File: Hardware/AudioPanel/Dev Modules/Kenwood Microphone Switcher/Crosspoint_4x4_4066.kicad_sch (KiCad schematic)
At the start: 14 parts, among them U106 4066, U107 4066, U108 4066, U51 4066, U53 4066, U55 4066

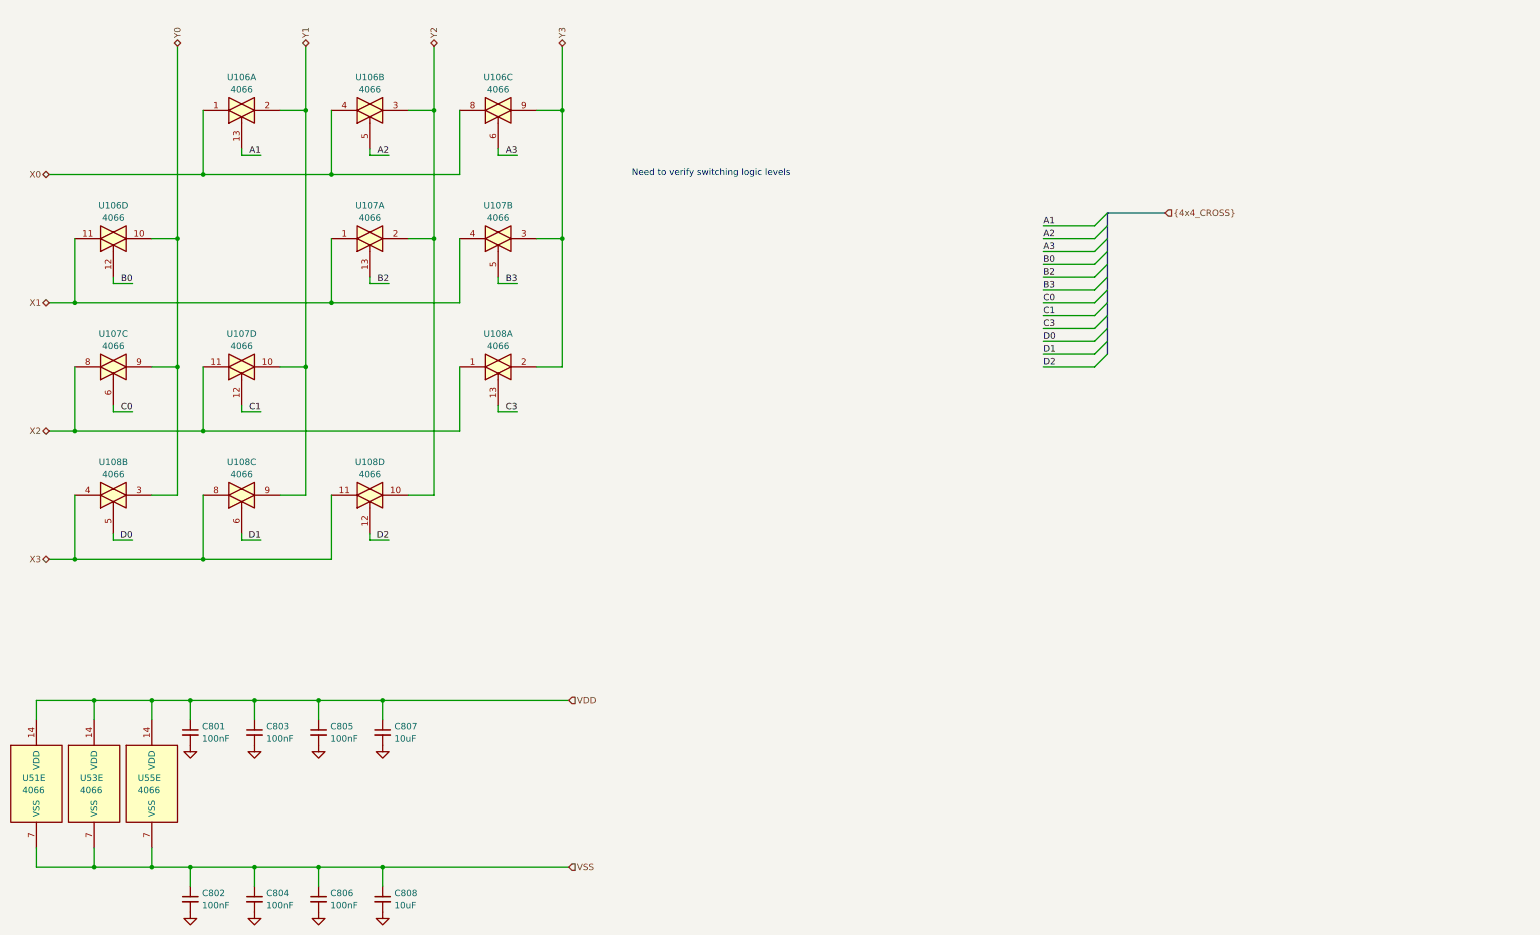
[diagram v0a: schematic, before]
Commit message: Finished most if not all of the microphone dev board
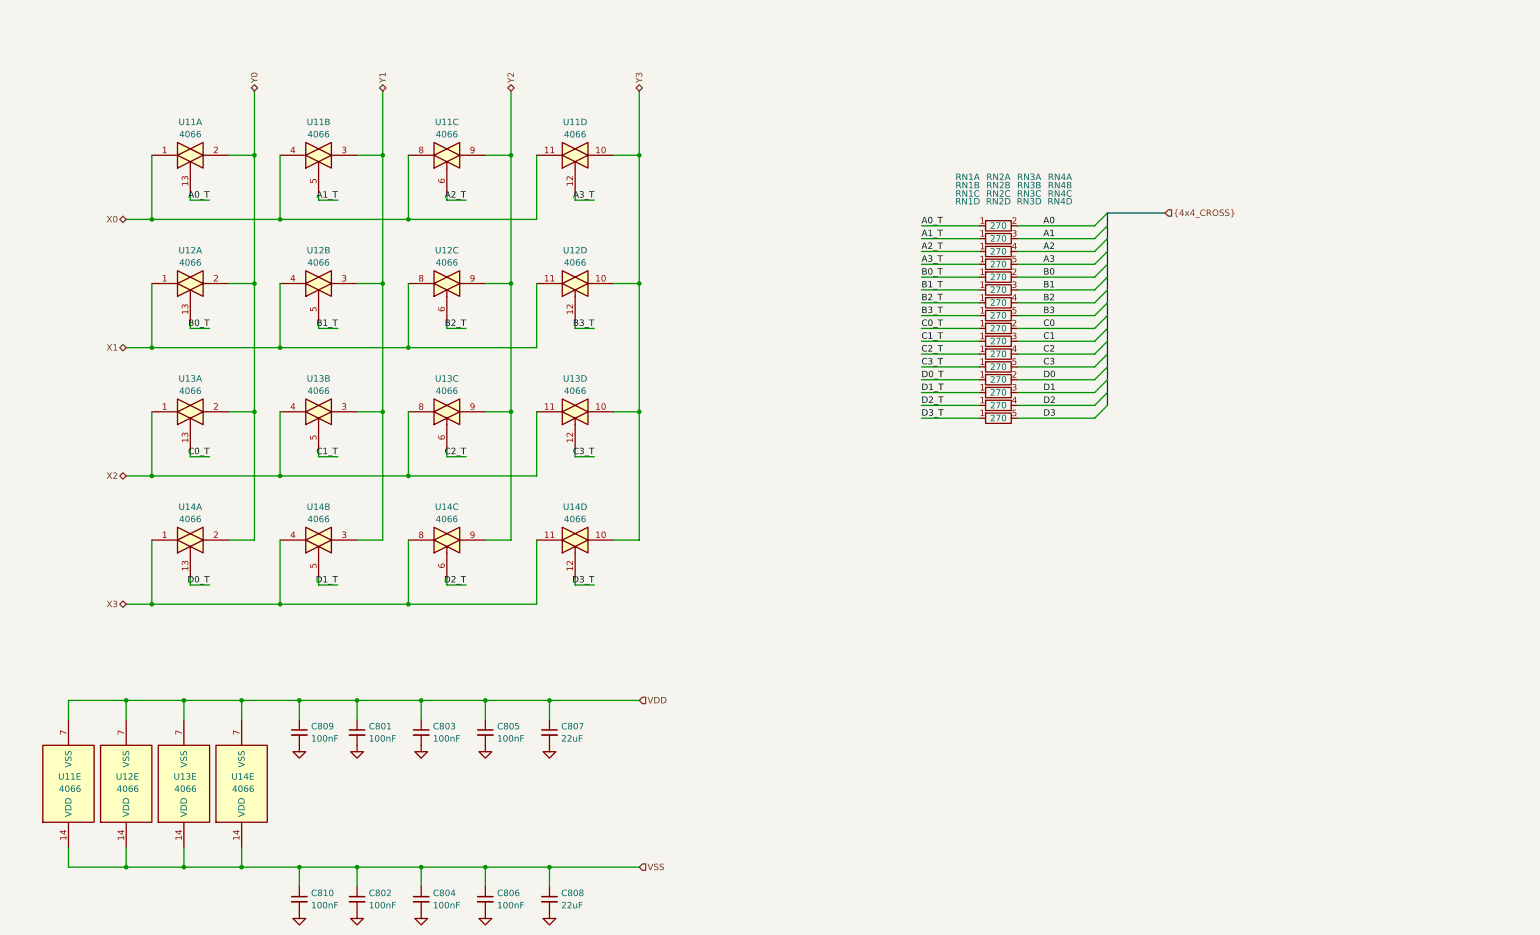
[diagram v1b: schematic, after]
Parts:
- removed U106, U107, U108, U51, U53, U55: 4066, symbol 4xxx:4066
- added C809, C810: 100nF, symbol Device:C_Small
- added RN1, RN2, RN3, RN4: 270, Resistor_THT:R_Array_SIP5, symbol Device:R_Network04_Split
- added U11, U12, U13, U14: 4066, symbol 4xxx:4066
- C807, C808: value 10uF -> 22uF
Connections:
- net A1: now also RN1.3 (R2.2)
- net A2: now also RN1.4 (R3.2)
- net A3: now also RN1.5 (R4.2)
- net B0: now also RN2.2 (R1.2)
- net B2: now also RN2.4 (R3.2)
- net B3: now also RN2.5 (R4.2)
- net C0: now also RN3.2 (R1.2)
- net C1: now also RN3.3 (R2.2)
- net C3: now also RN3.5 (R4.2)
- net D0: now also RN4.2 (R1.2)
- net D1: now also RN4.3 (R2.2)
- net D2: now also RN4.4 (R3.2)
- net GND: now also C809.2, C810.2
- net VDD: now also C809.1, U11.7 (VSS), U12.7 (VSS), U13.7 (VSS), U14.7 (VSS)
- net VSS: now also C810.1, U11.14 (VDD), U12.14 (VDD), U13.14 (VDD), U14.14 (VDD)
- net X0: now also U11.1, U11.11, U11.4, U11.8
- net X1: now also U12.1, U12.11, U12.4, U12.8
- net X2: now also U13.1, U13.11, U13.4, U13.8
- net X3: now also U14.1, U14.11, U14.4, U14.8
- net Y0: now also U11.2, U12.2, U13.2, U14.2
- net Y1: now also U11.3, U12.3, U13.3, U14.3
- net Y2: now also U11.9, U12.9, U13.9, U14.9
- net Y3: now also U11.10, U12.10, U13.10, U14.10
- new net A0: RN1.2 (R1.2)
- new net A0_T: RN1.1 (R1), U11.13
- new net A1_T: RN1.1 (R1), U11.5
- new net A2_T: RN1.1 (R1), U11.6
- new net A3_T: RN1.1 (R1), U11.12
- new net B0_T: RN2.1 (R1), U12.13
- new net B1: RN2.3 (R2.2)
- new net B1_T: RN2.1 (R1), U12.5
- new net B2_T: RN2.1 (R1), U12.6
- new net B3_T: RN2.1 (R1), U12.12
- new net C0_T: RN3.1 (R1), U13.13
- new net C1_T: RN3.1 (R1), U13.5
- new net C2: RN3.4 (R3.2)
- new net C2_T: RN3.1 (R1), U13.6
- new net C3_T: RN3.1 (R1), U13.12
- new net D0_T: RN4.1 (R1), U14.13
- new net D1_T: RN4.1 (R1), U14.5
- new net D2_T: RN4.1 (R1), U14.6
- new net D3: RN4.5 (R4.2)
- new net D3_T: RN4.1 (R1), U14.12
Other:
- note removed: "Need to verify switching logic levels"
- moved on the sheet: C801, C802, C803, C804, C805, C806, C807, C808

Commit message: Removed DAC and buffers for PTT, added PTT LEDs and inverters
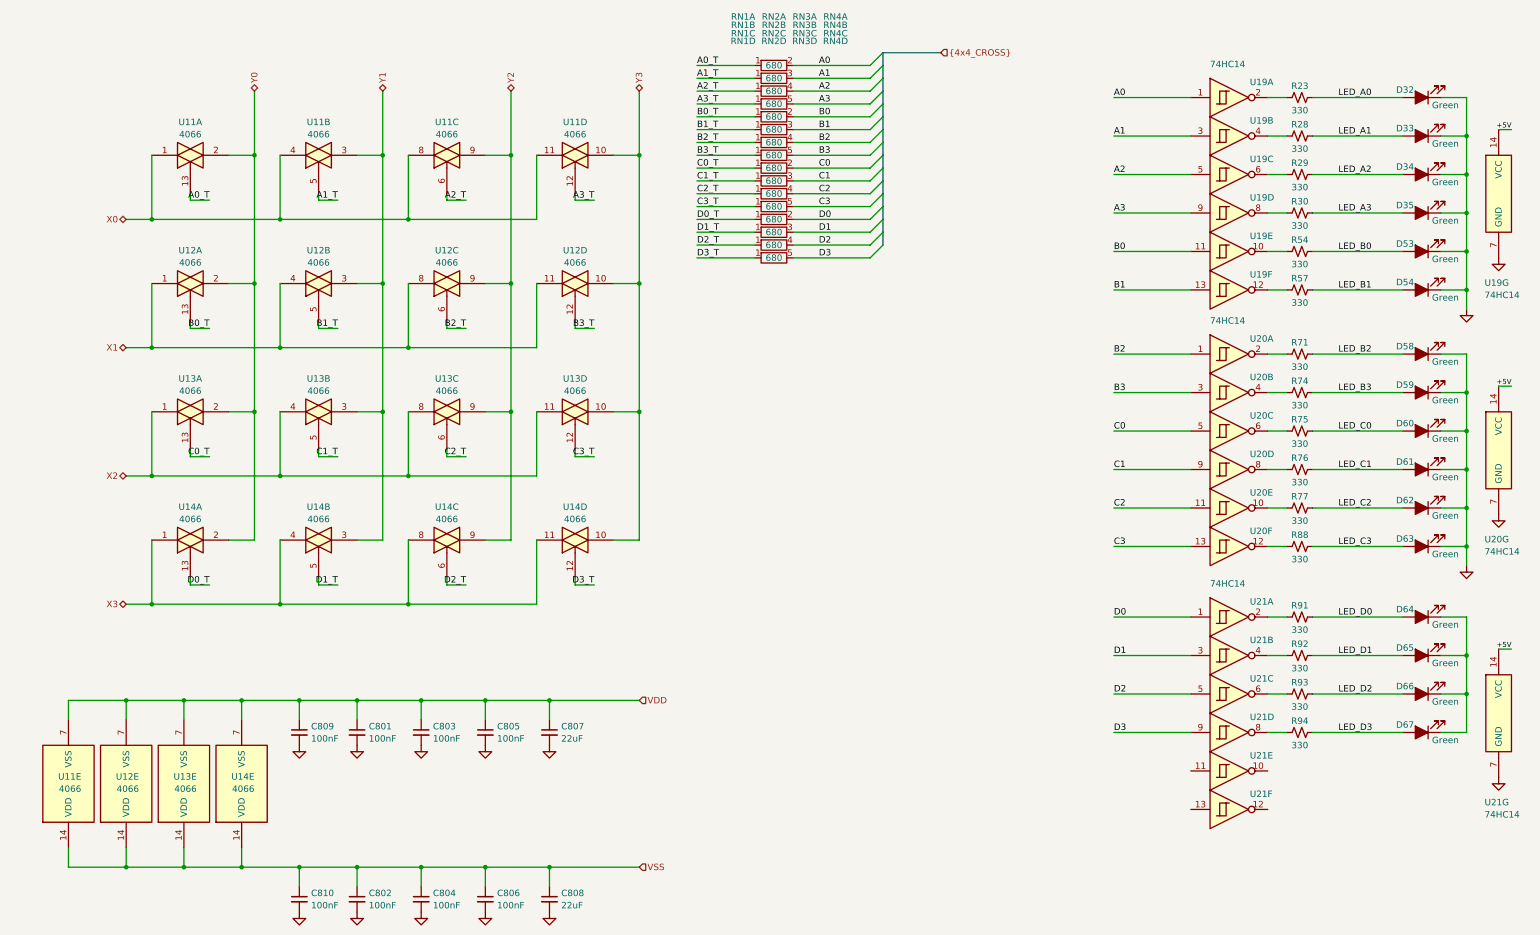
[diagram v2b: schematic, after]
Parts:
- added D32, D33, D34, D35, D53, D54, D58, D59, D60, D61, D62, D63, D64, D65, D66, D67: Green, LED_THT:LED_D5.0mm, symbol Device:LED_Filled
- added R23, R28, R29, R30, R54, R57, R71, R74, R75, R76, R77, R88, R91, R92, R93, R94: 330, symbol Device:R_Small_US
- added U19, U20, U21: 74HC14, symbol 74xx:74HC14
- RN1, RN2, RN3, RN4: value 270 -> 680
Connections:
- net A0: now also U19.1
- net A1: now also U19.3
- net A2: now also U19.5
- net A3: now also U19.9
- net B0: now also U19.11
- net B1: now also U19.13
- net B2: now also U20.1
- net B3: now also U20.3
- net C0: now also U20.5
- net C1: now also U20.9
- net C2: now also U20.11
- net C3: now also U20.13
- net D0: now also U21.1
- net D1: now also U21.3
- net D2: now also U21.5
- net D3: now also U21.9
- net GND: now also D32.1 (K), D33.1 (K), D34.1 (K), D35.1 (K), D53.1 (K), D54.1 (K), D58.1 (K), D59.1 (K), D60.1 (K), D61.1 (K), D62.1 (K), D63.1 (K), U19.7 (GND), U20.7 (GND), U21.7 (GND)
- new net: R57.2, U19.12
- new net: R71.2, U20.2
- new net: R92.2, U21.4
- new net: D64.1 (K), D65.1 (K), D66.1 (K), D67.1 (K)
- new net: R29.2, U19.6
- new net: R23.2, U19.2
- new net: R88.2, U20.12
- new net: R94.2, U21.8
- new net: R76.2, U20.8
- new net: R75.2, U20.6
- new net: R54.2, U19.10
- new net: R74.2, U20.4
- new net: R28.2, U19.4
- new net: R91.2, U21.2
- new net: R77.2, U20.10
- new net: R93.2, U21.6
- new net: R30.2, U19.8
- new net +5V: U19.14 (VCC), U20.14 (VCC), U21.14 (VCC)
- new net LED_A0: D32.2 (A), R23.1
- new net LED_A1: D33.2 (A), R28.1
- new net LED_A2: D34.2 (A), R29.1
- new net LED_A3: D35.2 (A), R30.1
- new net LED_B0: D53.2 (A), R54.1
- new net LED_B1: D54.2 (A), R57.1
- new net LED_B2: D58.2 (A), R71.1
- new net LED_B3: D59.2 (A), R74.1
- new net LED_C0: D60.2 (A), R75.1
- new net LED_C1: D61.2 (A), R76.1
- new net LED_C2: D62.2 (A), R77.1
- new net LED_C3: D63.2 (A), R88.1
- new net LED_D0: D64.2 (A), R91.1
- new net LED_D1: D65.2 (A), R92.1
- new net LED_D2: D66.2 (A), R93.1
- new net LED_D3: D67.2 (A), R94.1
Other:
- moved on the sheet: RN1A, RN1B, RN1C, RN1D, RN2A, RN2B, RN2C, RN2D, RN3A, RN3B, RN3C, RN3D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

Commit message: Assigned (most) footprints
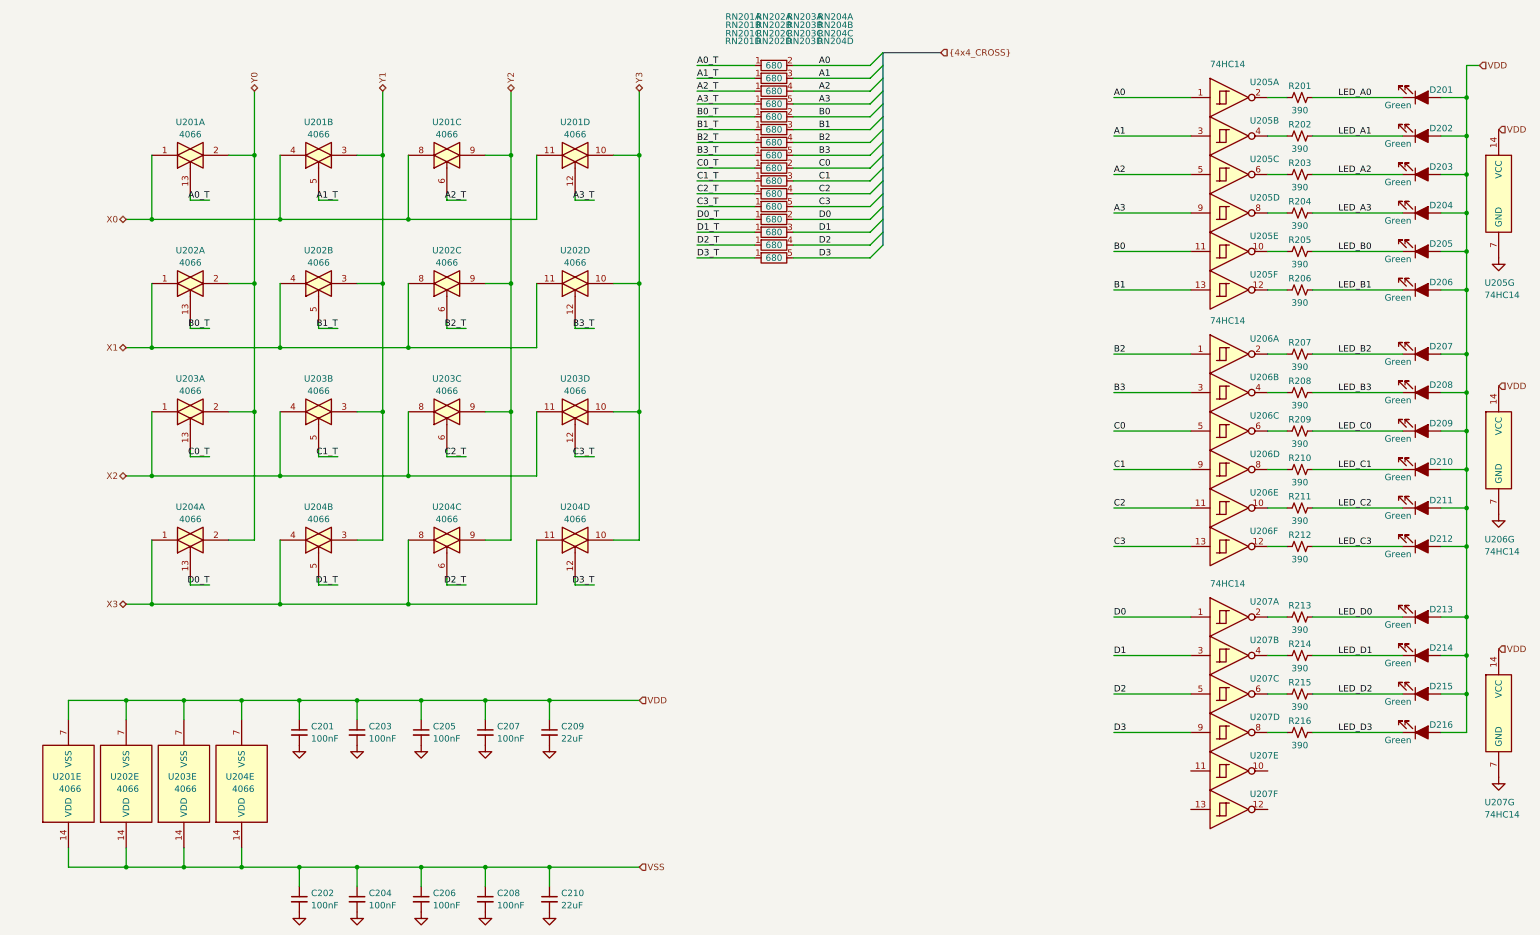
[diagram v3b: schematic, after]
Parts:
- C201: renamed from C809; footprint (none) -> Capacitor_SMD:C_0402_1005Metric
- C202: renamed from C810; footprint (none) -> Capacitor_SMD:C_0402_1005Metric
- C203: renamed from C801; footprint (none) -> Capacitor_SMD:C_0402_1005Metric
- C204: renamed from C802; footprint (none) -> Capacitor_SMD:C_0402_1005Metric
- C205: renamed from C803; footprint (none) -> Capacitor_SMD:C_0402_1005Metric
- C206: renamed from C804; footprint (none) -> Capacitor_SMD:C_0402_1005Metric
- C207: renamed from C805; footprint (none) -> Capacitor_SMD:C_0402_1005Metric
- C208: renamed from C806; footprint (none) -> Capacitor_SMD:C_0402_1005Metric
- C209: renamed from C807; footprint (none) -> Capacitor_SMD:C_0603_1608Metric
- C210: renamed from C808; footprint (none) -> Capacitor_SMD:C_0603_1608Metric
- R201: renamed from R23; value 330 -> 390; footprint (none) -> Resistor_SMD:R_0402_1005Metric
- R202: renamed from R28; value 330 -> 390; footprint (none) -> Resistor_SMD:R_0402_1005Metric
- R203: renamed from R29; value 330 -> 390; footprint (none) -> Resistor_SMD:R_0402_1005Metric
- R204: renamed from R30; value 330 -> 390; footprint (none) -> Resistor_SMD:R_0402_1005Metric
- R205: renamed from R54; value 330 -> 390; footprint (none) -> Resistor_SMD:R_0402_1005Metric
- R206: renamed from R57; value 330 -> 390; footprint (none) -> Resistor_SMD:R_0402_1005Metric
- R207: renamed from R71; value 330 -> 390; footprint (none) -> Resistor_SMD:R_0402_1005Metric
- R208: renamed from R74; value 330 -> 390; footprint (none) -> Resistor_SMD:R_0402_1005Metric
- R209: renamed from R75; value 330 -> 390; footprint (none) -> Resistor_SMD:R_0402_1005Metric
- R210: renamed from R76; value 330 -> 390; footprint (none) -> Resistor_SMD:R_0402_1005Metric
- R211: renamed from R77; value 330 -> 390; footprint (none) -> Resistor_SMD:R_0402_1005Metric
- R212: renamed from R88; value 330 -> 390; footprint (none) -> Resistor_SMD:R_0402_1005Metric
- R213: renamed from R91; value 330 -> 390; footprint (none) -> Resistor_SMD:R_0402_1005Metric
- R214: renamed from R92; value 330 -> 390; footprint (none) -> Resistor_SMD:R_0402_1005Metric
- R215: renamed from R93; value 330 -> 390; footprint (none) -> Resistor_SMD:R_0402_1005Metric
- R216: renamed from R94; value 330 -> 390; footprint (none) -> Resistor_SMD:R_0402_1005Metric
- U201: renamed from U11; footprint (none) -> Package_SO:SOIC-14_3.9x8.7mm_P1.27mm
- U202: renamed from U12; footprint (none) -> Package_SO:SOIC-14_3.9x8.7mm_P1.27mm
- U203: renamed from U13; footprint (none) -> Package_SO:SOIC-14_3.9x8.7mm_P1.27mm
- U204: renamed from U14; footprint (none) -> Package_SO:SOIC-14_3.9x8.7mm_P1.27mm
- U205: renamed from U19; footprint (none) -> Package_SO:SOIC-14_3.9x8.7mm_P1.27mm
- U206: renamed from U20; footprint (none) -> Package_SO:SOIC-14_3.9x8.7mm_P1.27mm
- U207: renamed from U21; footprint (none) -> Package_SO:SOIC-14_3.9x8.7mm_P1.27mm
- renumbered D32 to D201, D33 to D202, D34 to D203, D35 to D204, D53 to D205, D54 to D206, D58 to D207, D59 to D208, D60 to D209, D61 to D210, D62 to D211, D63 to D212, D64 to D213, D65 to D214, D66 to D215, D67 to D216, RN1 to RN201, RN2 to RN202, RN3 to RN203, RN4 to RN204
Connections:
- net +5V is gone; now on net VDD: U205.14 (VCC), U206.14 (VCC), U207.14 (VCC)
- net GND: no longer D201.1 (K), D202.1 (K), D203.1 (K), D204.1 (K), D205.1 (K), D206.1 (K), D207.1 (K), D208.1 (K), D209.1 (K), D210.1 (K), D211.1 (K), D212.1 (K)
- net LED_A0: now also D201.1 (K); no longer D201.2 (A)
- net LED_A1: now also D202.1 (K); no longer D202.2 (A)
- net LED_A2: now also D203.1 (K); no longer D203.2 (A)
- net LED_A3: now also D204.1 (K); no longer D204.2 (A)
- net LED_B0: now also D205.1 (K); no longer D205.2 (A)
- net LED_B1: now also D206.1 (K); no longer D206.2 (A)
- net LED_B2: now also D207.1 (K); no longer D207.2 (A)
- net LED_B3: now also D208.1 (K); no longer D208.2 (A)
- net LED_C0: now also D209.1 (K); no longer D209.2 (A)
- net LED_C1: now also D210.1 (K); no longer D210.2 (A)
- net LED_C2: now also D211.1 (K); no longer D211.2 (A)
- net LED_C3: now also D212.1 (K); no longer D212.2 (A)
- net LED_D0: now also D213.1 (K); no longer D213.2 (A)
- net LED_D1: now also D214.1 (K); no longer D214.2 (A)
- net LED_D2: now also D215.1 (K); no longer D215.2 (A)
- net LED_D3: now also D216.1 (K); no longer D216.2 (A)
- net VDD: now also D201.2 (A), D202.2 (A), D203.2 (A), D204.2 (A), D205.2 (A), D206.2 (A), D207.2 (A), D208.2 (A), D209.2 (A), D210.2 (A), D211.2 (A), D212.2 (A), D213.2 (A), D214.2 (A), D215.2 (A), D216.2 (A)
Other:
- moved on the sheet: D201, D202, D203, D204, D205, D206, D207, D208, D209, D210, D211, D212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
